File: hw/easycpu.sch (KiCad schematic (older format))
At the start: 0 parts

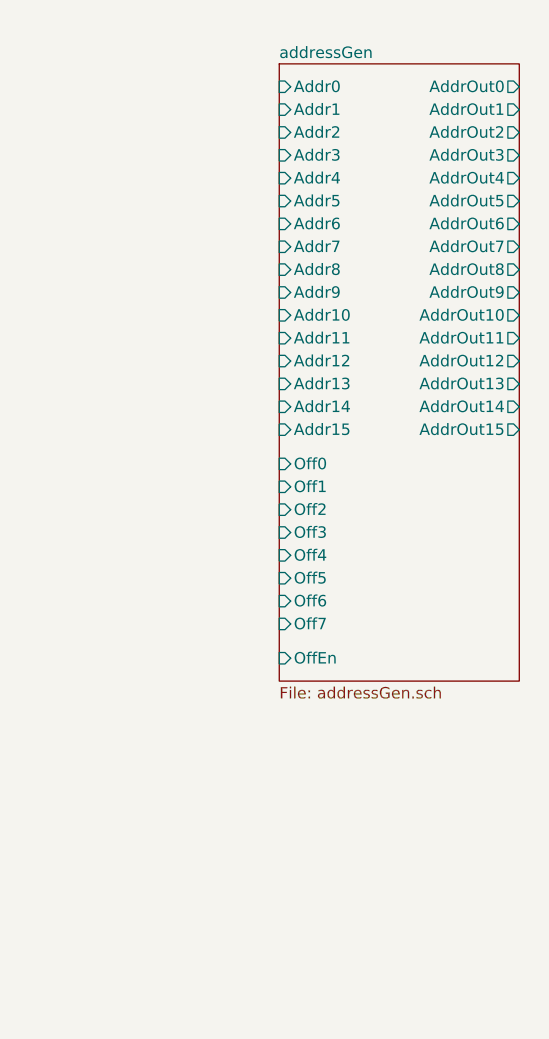
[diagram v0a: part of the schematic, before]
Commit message: added ALo/AHi output buffers to addrGen unit
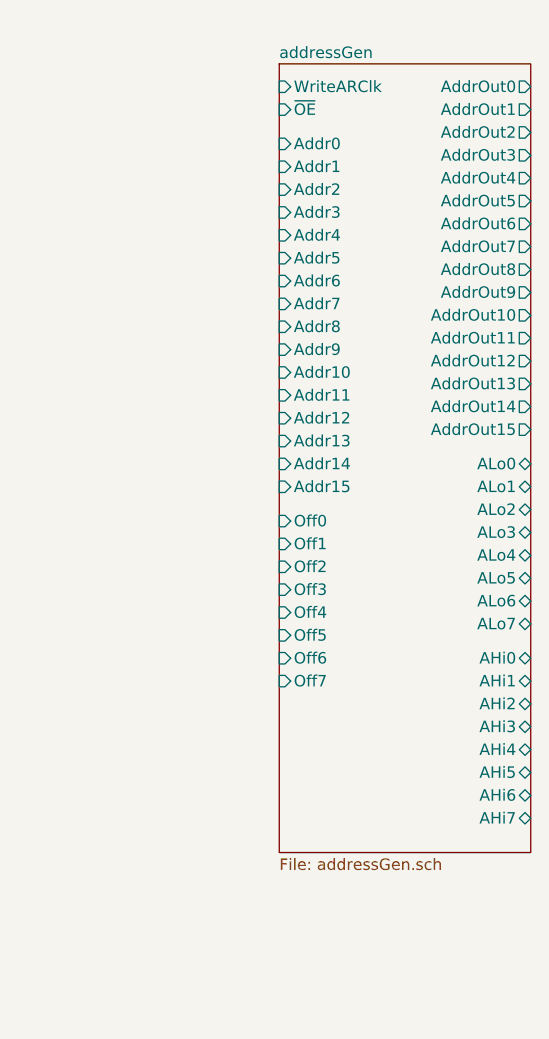
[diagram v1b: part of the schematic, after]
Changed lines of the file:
@@
 EESchema Schematic File Version 4
 LIBS:easycpu-cache
-EELAYER 26 0
+EELAYER 30 0
 EELAYER END
 $Descr User 13750 10625
@@
 Comment4 ""
 $EndDescr
-$Sheet
-S 9750 1400 1050 2700
-U 5D98FACA
-F0 "addressGen" 50
-F1 "addressGen.sch" 50
-F2 "Addr0" I L 9750 1500 50
-F3 "Addr1" I L 9750 1600 50
-F4 "Addr2" I L 9750 1700 50
-F5 "Addr3" I L 9750 1800 50
-F6 "Addr4" I L 9750 1900 50
-F7 "Addr5" I L 9750 2000 50
-F8 "Addr6" I L 9750 2100 50
-F9 "Addr7" I L 9750 2200 50
-F10 "Addr8" I L 9750 2300 50
-F11 "Addr9" I L 9750 2400 50
-F12 "Addr10" I L 9750 2500 50
-F13 "Addr11" I L 9750 2600 50
-F14 "Addr12" I L 9750 2700 50
-F15 "Addr13" I L 9750 2800 50
-F16 "Addr14" I L 9750 2900 50
-F17 "Addr15" I L 9750 3000 50
-F18 "Off0" I L 9750 3150 50
-F19 "Off1" I L 9750 3250 50
-F20 "Off2" I L 9750 3350 50
-F21 "Off3" I L 9750 3450 50
-F22 "Off4" I L 9750 3550 50
-F23 "Off5" I L 9750 3650 50
-F24 "Off6" I L 9750 3750 50
-F25 "Off7" I L 9750 3850 50
-F26 "OffEn" I L 9750 4000 50
-F27 "AddrOut0" O R 10800 1500 50
-F28 "AddrOut1" O R 10800 1600 50
-F29 "AddrOut2" O R 10800 1700 50
-F30 "AddrOut3" O R 10800 1800 50
-F31 "AddrOut4" O R 10800 1900 50
-F32 "AddrOut5" O R 10800 2000 50
-F33 "AddrOut6" O R 10800 2100 50
-F34 "AddrOut7" O R 10800 2200 50
-F35 "AddrOut8" O R 10800 2300 50
-F36 "AddrOut9" O R 10800 2400 50
-F37 "AddrOut10" O R 10800 2500 50
-F38 "AddrOut11" O R 10800 2600 50
-F39 "AddrOut12" O R 10800 2700 50
-F40 "AddrOut13" O R 10800 2800 50
-F41 "AddrOut14" O R 10800 2900 50
-F42 "AddrOut15" O R 10800 3000 50
-$EndSheet
 Text Notes 9100 9100 0    50   ~ 0
 Easy 8-bit CPU
@@
 F36 "~ALUOE" I L 7150 7550 50
 $EndSheet
+$Sheet
+S 9750 1400 1100 3450
+U 5D98FACA
+F0 "addressGen" 50
+F1 "addressGen.sch" 50
+F2 "Addr0" I L 9750 1750 50
+F3 "Addr1" I L 9750 1850 50
+F4 "Addr2" I L 9750 1950 50
+F5 "Addr3" I L 9750 2050 50
+F6 "Addr4" I L 9750 2150 50
+F7 "Addr5" I L 9750 2250 50
+F8 "Addr6" I L 9750 2350 50
+F9 "Addr7" I L 9750 2450 50
+F10 "Addr8" I L 9750 2550 50
+F11 "Addr9" I L 9750 2650 50
+F12 "Addr10" I L 9750 2750 50
+F13 "Addr11" I L 9750 2850 50
+F14 "Addr12" I L 9750 2950 50
+F15 "Addr13" I L 9750 3050 50
+F16 "Addr14" I L 9750 3150 50
+F17 "Addr15" I L 9750 3250 50
+F18 "Off0" I L 9750 3400 50
+F19 "Off1" I L 9750 3500 50
+F20 "Off2" I L 9750 3600 50
+F21 "Off3" I L 9750 3700 50
+F22 "Off4" I L 9750 3800 50
+F23 "Off5" I L 9750 3900 50
+F24 "Off6" I L 9750 4000 50
+F25 "Off7" I L 9750 4100 50
+F26 "AddrOut0" O R 10850 1500 50
+F27 "AddrOut1" O R 10850 1600 50
+F28 "AddrOut2" O R 10850 1700 50
+F29 "AddrOut3" O R 10850 1800 50
+F30 "AddrOut4" O R 10850 1900 50
+F31 "AddrOut5" O R 10850 2000 50
+F32 "AddrOut6" O R 10850 2100 50
+F33 "AddrOut7" O R 10850 2200 50
+F34 "AddrOut8" O R 10850 2300 50
+F35 "AddrOut9" O R 10850 2400 50
+F36 "AddrOut10" O R 10850 2500 50
+F37 "AddrOut11" O R 10850 2600 50
+F38 "AddrOut12" O R 10850 2700 50
+F39 "AddrOut13" O R 10850 2800 50
+F40 "AddrOut14" O R 10850 2900 50
+F41 "AddrOut15" O R 10850 3000 50
+F42 "WriteARClk" I L 9750 1500 50
+F43 "ALo0" T R 10850 3150 50
+F44 "ALo1" T R 10850 3250 50
+F45 "ALo2" T R 10850 3350 50
+F46 "ALo3" T R 10850 3450 50
+F47 "ALo4" T R 10850 3550 50
+F48 "ALo5" T R 10850 3650 50
+F49 "ALo6" T R 10850 3750 50
+F50 "ALo7" T R 10850 3850 50
+F51 "AHi0" T R 10850 4000 50
+F52 "AHi1" T R 10850 4100 50
+F53 "AHi2" T R 10850 4200 50
+F54 "AHi3" T R 10850 4300 50
+F55 "AHi4" T R 10850 4400 50
+F56 "AHi5" T R 10850 4500 50
+F57 "AHi6" T R 10850 4600 50
+F58 "AHi7" T R 10850 4700 50
+F59 "~OE" I L 9750 1600 50
+$EndSheet
 $EndSCHEMATC

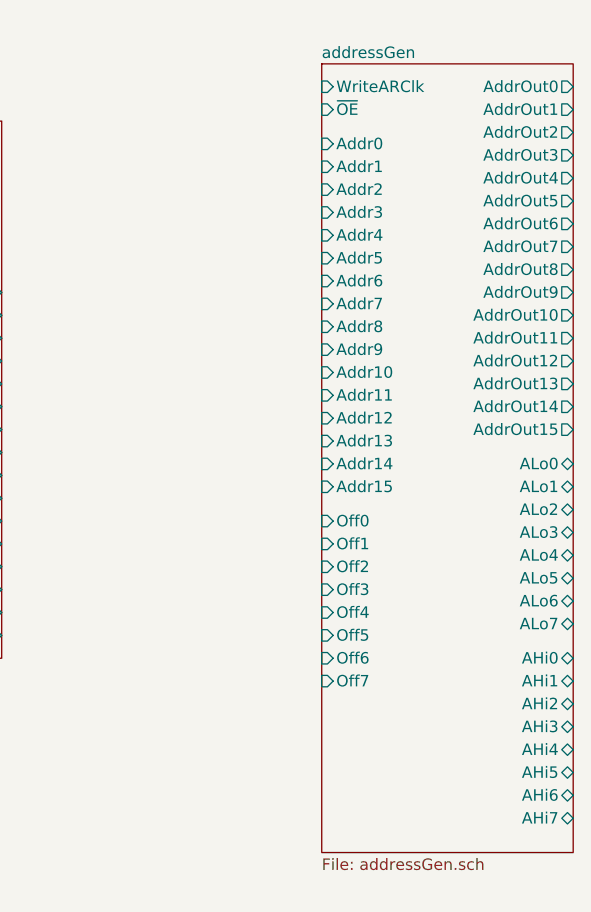
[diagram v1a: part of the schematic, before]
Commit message: generation of 0 and 1 constant offsets in addrGen
Also added pullup resistors to the offset bus to ensure
inputs are valid and also to implicitly generate the
-1 constant offset.
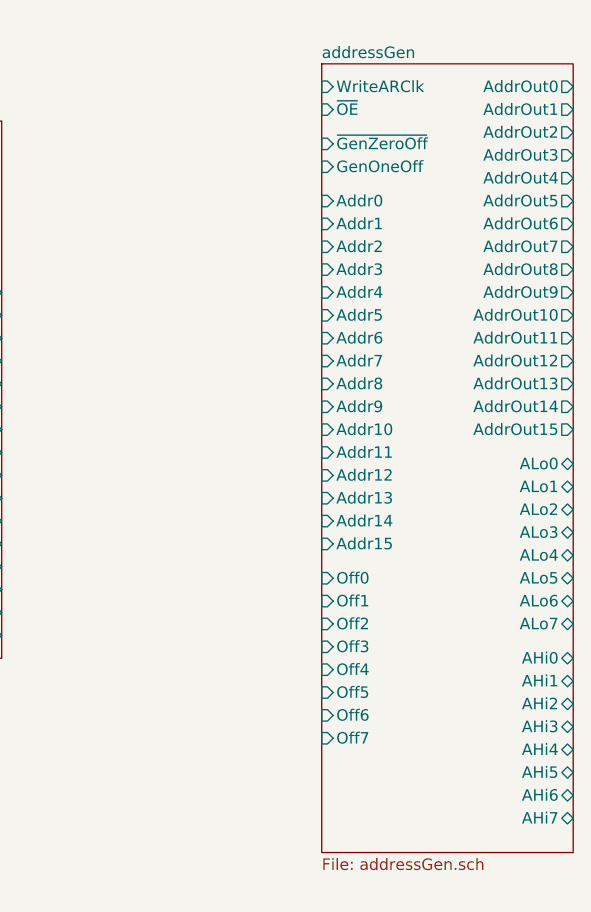
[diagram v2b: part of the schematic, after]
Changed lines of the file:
@@
 F0 "addressGen" 50
 F1 "addressGen.sch" 50
-F2 "Addr0" I L 9750 1750 50
-F3 "Addr1" I L 9750 1850 50
-F4 "Addr2" I L 9750 1950 50
-F5 "Addr3" I L 9750 2050 50
-F6 "Addr4" I L 9750 2150 50
-F7 "Addr5" I L 9750 2250 50
-F8 "Addr6" I L 9750 2350 50
-F9 "Addr7" I L 9750 2450 50
-F10 "Addr8" I L 9750 2550 50
-F11 "Addr9" I L 9750 2650 50
-F12 "Addr10" I L 9750 2750 50
-F13 "Addr11" I L 9750 2850 50
-F14 "Addr12" I L 9750 2950 50
-F15 "Addr13" I L 9750 3050 50
-F16 "Addr14" I L 9750 3150 50
-F17 "Addr15" I L 9750 3250 50
-F18 "Off0" I L 9750 3400 50
-F19 "Off1" I L 9750 3500 50
-F20 "Off2" I L 9750 3600 50
-F21 "Off3" I L 9750 3700 50
-F22 "Off4" I L 9750 3800 50
-F23 "Off5" I L 9750 3900 50
-F24 "Off6" I L 9750 4000 50
-F25 "Off7" I L 9750 4100 50
+F2 "Addr0" I L 9750 2000 50
+F3 "Addr1" I L 9750 2100 50
+F4 "Addr2" I L 9750 2200 50
+F5 "Addr3" I L 9750 2300 50
+F6 "Addr4" I L 9750 2400 50
+F7 "Addr5" I L 9750 2500 50
+F8 "Addr6" I L 9750 2600 50
+F9 "Addr7" I L 9750 2700 50
+F10 "Addr8" I L 9750 2800 50
+F11 "Addr9" I L 9750 2900 50
+F12 "Addr10" I L 9750 3000 50
+F13 "Addr11" I L 9750 3100 50
+F14 "Addr12" I L 9750 3200 50
+F15 "Addr13" I L 9750 3300 50
+F16 "Addr14" I L 9750 3400 50
+F17 "Addr15" I L 9750 3500 50
+F18 "Off0" I L 9750 3650 50
+F19 "Off1" I L 9750 3750 50
+F20 "Off2" I L 9750 3850 50
+F21 "Off3" I L 9750 3950 50
+F22 "Off4" I L 9750 4050 50
+F23 "Off5" I L 9750 4150 50
+F24 "Off6" I L 9750 4250 50
+F25 "Off7" I L 9750 4350 50
 F26 "AddrOut0" O R 10850 1500 50
 F27 "AddrOut1" O R 10850 1600 50
@@
 F58 "AHi7" T R 10850 4700 50
 F59 "~OE" I L 9750 1600 50
+F60 "~GenZeroOff" I L 9750 1750 50
+F61 "GenOneOff" I L 9750 1850 50
 $EndSheet
 $EndSCHEMATC
